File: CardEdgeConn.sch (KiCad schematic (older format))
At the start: 1 part

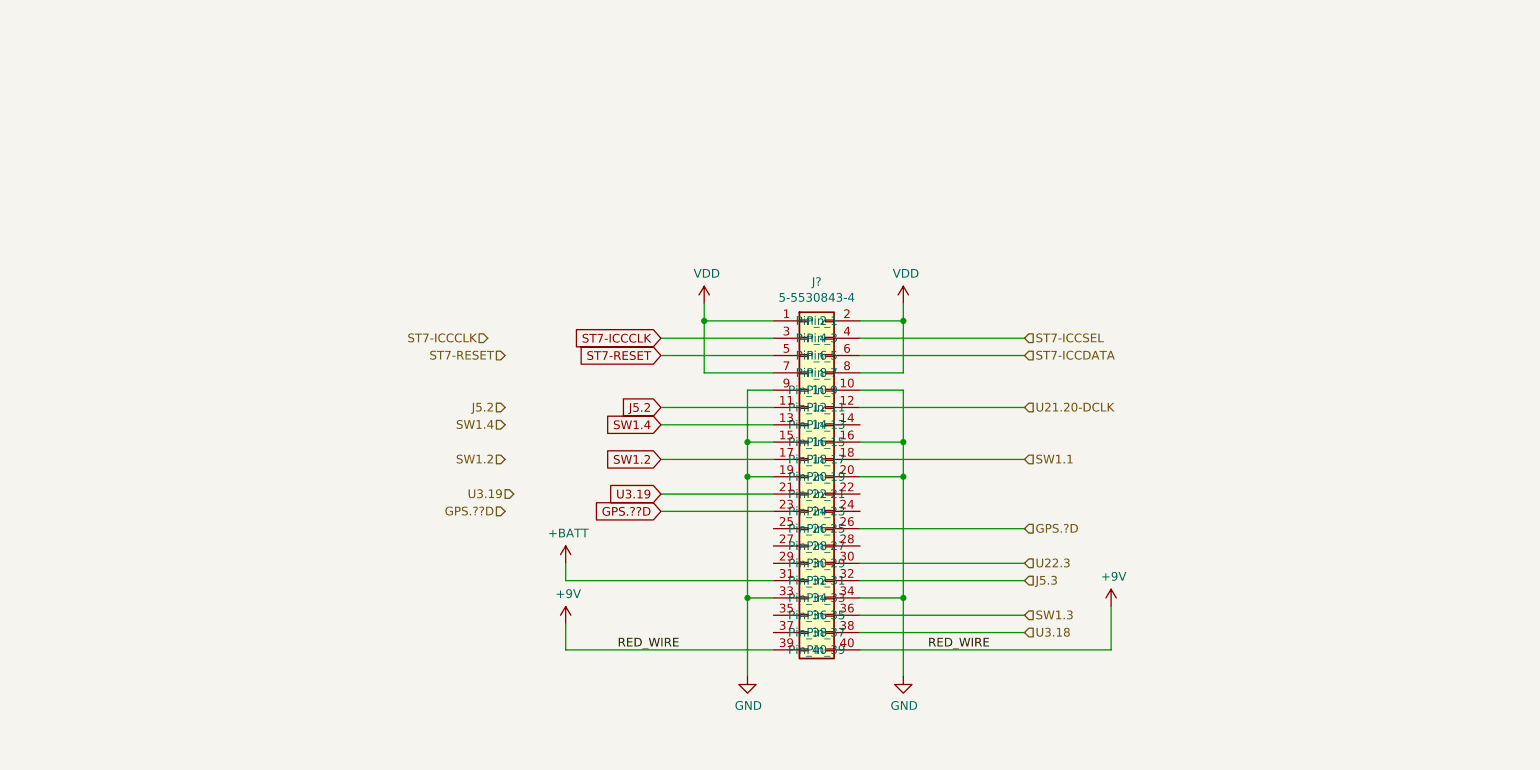
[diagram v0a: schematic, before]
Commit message: Added DC-DC converter
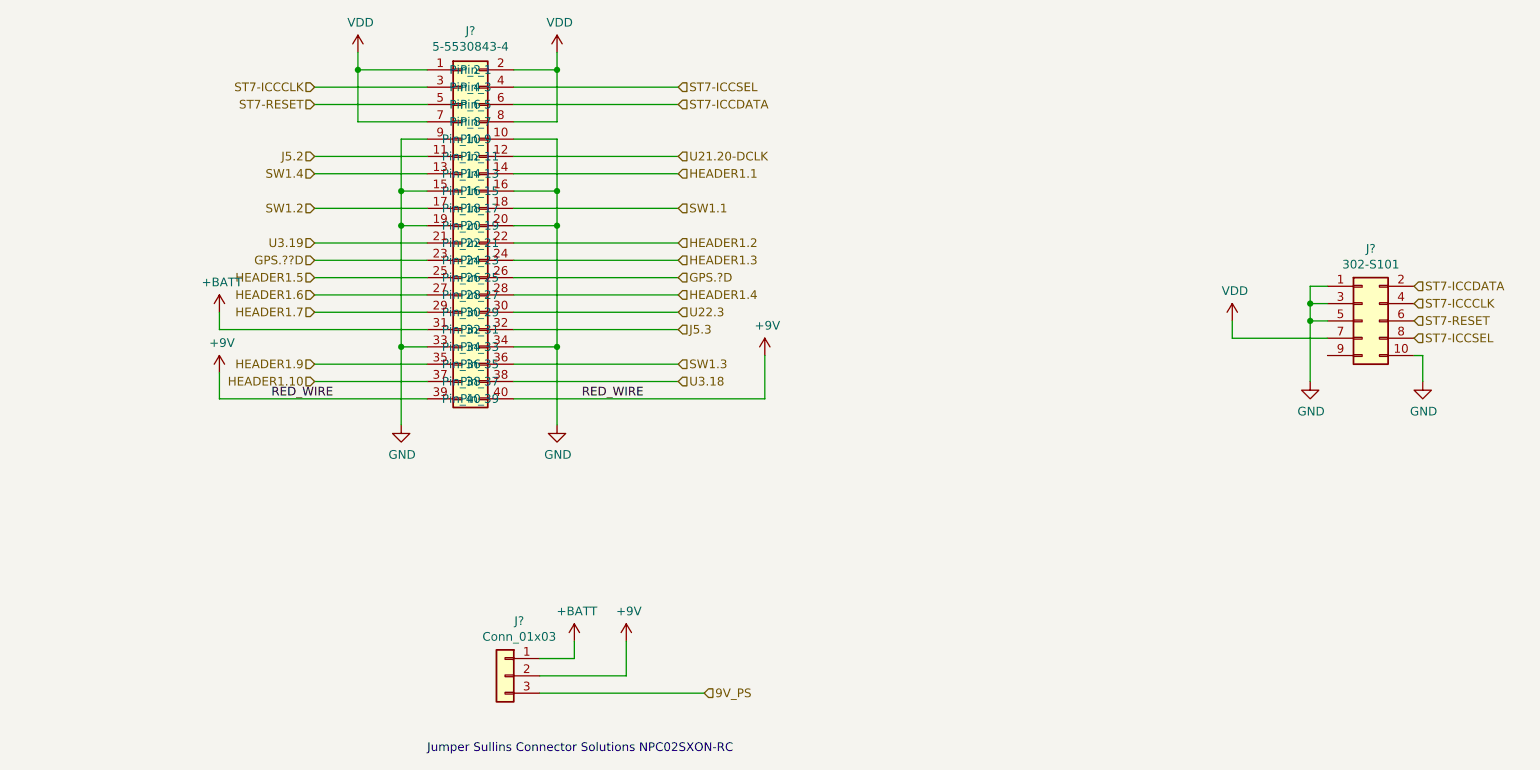
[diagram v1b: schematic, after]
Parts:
- added J?: 302-S101, digikey-footprints:PinHeader_2x5_P2.54mm_Drill1.2mm, symbol Connector_Generic:Conn_02x05_Odd_Even
- added J?: Conn_01x03, symbol Connector_Generic:Conn_01x03
- J?: MPN (none) -> 5-5530843-4; Manufacturer (none) -> TE Connectivity AMP Connectors
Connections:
- net +9V: now also J?.2 (Pin_2)
- net +BATT: now also J?.1 (Pin_1)
- net GND: now also J?.1 (Pin_1), J?.10 (Pin_10), J?.3 (Pin_3), J?.5 (Pin_5)
- net ST7-ICCCLK: now also J?.4 (Pin_4)
- net ST7-ICCDATA: now also J?.2 (Pin_2)
- net ST7-ICCSEL: now also J?.8 (Pin_8)
- net ST7-RESET: now also J?.6 (Pin_6)
- net VDD: now also J?.7 (Pin_7)
- net HEADER1.1: now reaches J?.14 (Pin_14)
- net HEADER1.2: now reaches J?.22 (Pin_22)
- net HEADER1.3: now reaches J?.24 (Pin_24)
- net HEADER1.5: now reaches J?.25 (Pin_25)
- net HEADER1.6: now reaches J?.27 (Pin_27)
- net HEADER1.4: now reaches J?.28 (Pin_28)
- net HEADER1.7: now reaches J?.29 (Pin_29)
- net HEADER1.9: now reaches J?.35 (Pin_35)
- net HEADER1.10: now reaches J?.37 (Pin_37)
- new net 9V_PS: J?.3 (Pin_3)
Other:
- note added: "Jumper Sullins Connector Solutions NPC02SXON-RC"
- moved on the sheet: J?

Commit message: Added libraries used in the project. Top level connections.
Added libraries used in this project to the project folder.

Made additonal top level connections on the top level schematic.
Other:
- note added: "Jumper Sullins Connector Solutions NPC02SXON-RC\nJumper 1-2 to power from LMS6 Battery\nJumper 2-3 to power from exteral power"
- note removed: "Jumper Sullins Connector Solutions NPC02SXON-RC"
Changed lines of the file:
@@
 	4500 4800 3550 4800
 Text Notes 2900 5150 0    50   ~ 0
-Jumper Sullins Connector Solutions NPC02SXON-RC
+Jumper Sullins Connector Solutions NPC02SXON-RC\nJumper 1-2 to power from LMS6 Battery\nJumper 2-3 to power from exteral power
 $EndSCHEMATC

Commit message: Updated EdgeCardConn.sch with GPS UART
Confiremed the GPS UART pins from discord chat.
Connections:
- net GPS.??D renamed GPS.TXD
- net GPS.?D renamed GPS.RXD
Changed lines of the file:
@@
 	2250 2300 2900 2300
 Wire Wire Line
-	1700 2700 2900 2700
-Wire Wire Line
-	1700 2600 1700 2700
+	1500 2600 1500 2700
 $Comp
 L power:+BATT #PWR?
 U 1 1 5F7D097E
-P 1700 2600
+P 1500 2600
 AR Path="/5F7D097E" Ref="#PWR?"  Part="1"
 AR Path="/5F7BE189/5F7D097E" Ref="#PWR?"  Part="1"
 AR Path="/5F7C6408/5F7D097E" Ref="#PWR0103"  Part="1"
-F 0 "#PWR0103" H 1700 2450 50  0001 C CNN
-F 1 "+BATT" H 1715 2773 50  0000 C CNN
-F 2 "" H 1700 2600 50  0001 C CNN
-F 3 "" H 1700 2600 50  0001 C CNN
-	1    1700 2600
+F 0 "#PWR0103" H 1500 2450 50  0001 C CNN
+F 1 "+BATT" H 1515 2773 50  0000 C CNN
+F 2 "" H 1500 2600 50  0001 C CNN
+F 3 "" H 1500 2600 50  0001 C CNN
+	1    1500 2600
 	1    0    0    -1
 $EndComp
@@
 SW1.1
 Text HLabel 4350 2400 2    50   Input ~ 0
-GPS.?D
+GPS.RXD
 Text HLabel 4350 2600 2    50   Input ~ 0
 U22.3
@@
 U3.18
 Text HLabel 2250 2300 0    50   Input ~ 0
-GPS.??D
+GPS.TXD
 Text HLabel 2250 2200 0    50   Input ~ 0
 U3.19
@@
 Text Notes 2900 5150 0    50   ~ 0
 Jumper Sullins Connector Solutions NPC02SXON-RC\nJumper 1-2 to power from LMS6 Battery\nJumper 2-3 to power from exteral power
+Wire Wire Line
+	1500 2700 2900 2700
 $EndSCHEMATC

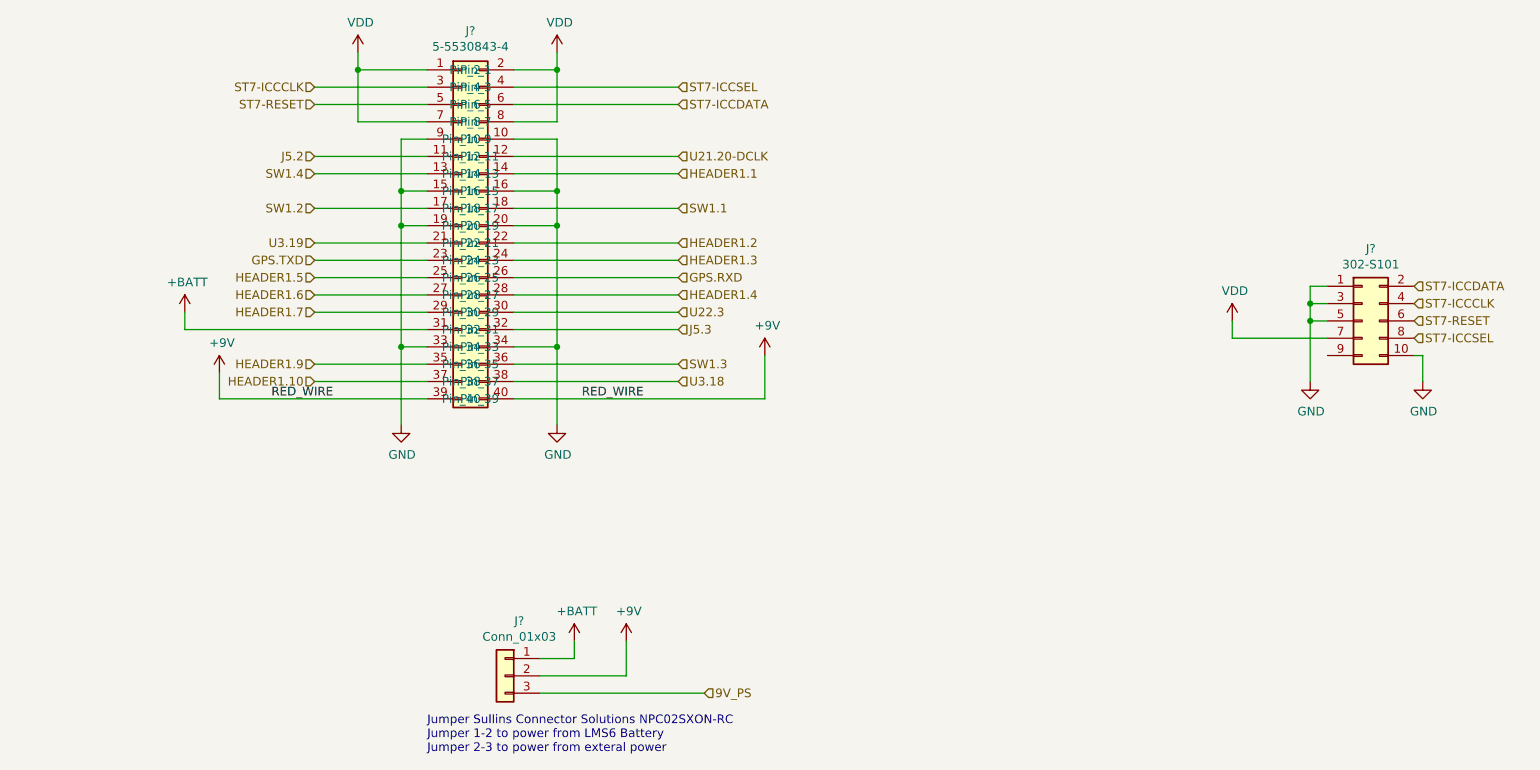
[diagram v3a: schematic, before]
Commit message: Annotated schematics and added UART Jumpers
Annotated schematics.

Added jumpers to GPS UART because I'm still not 100% sure on the connections and I don't want to have to respin a board because I was wrong.
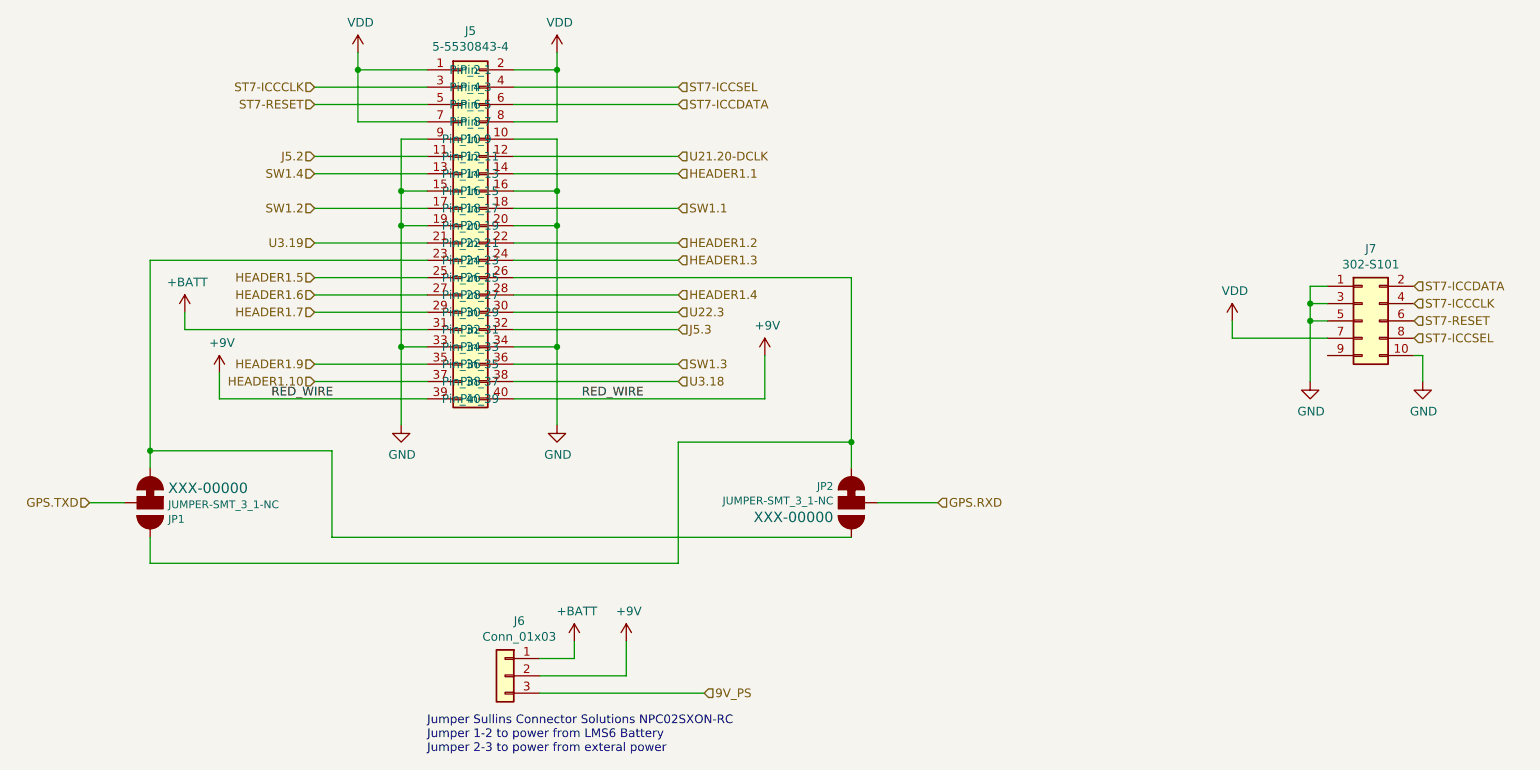
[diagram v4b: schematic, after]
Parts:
- added JP1, JP2: JUMPER-SMT_3_1-NC, SMT-JUMPER_3_1-NC, symbol SparkFun-Jumpers:JUMPER-SMT_3_1-NC
- gave numbers to parts that had none: 3
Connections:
- net GPS.RXD: now also JP2.2; no longer J5.26 (Pin_26)
- net GPS.TXD: now also JP1.2; no longer J5.23 (Pin_23)
- new net: J5.23 (Pin_23), JP1.3, JP2.1
- new net: J5.26 (Pin_26), JP1.1, JP2.3
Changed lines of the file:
@@
 $Descr A4 11693 8268
 encoding utf-8
-Sheet 2 4
+Sheet 4 4
 Title ""
 Date ""
@@
 	3400 2000 4350 2000
 Wire Wire Line
-	3400 2400 4350 2400
-Wire Wire Line
 	3400 2700 4350 2700
 Wire Wire Line
@@
 	2250 2200 2900 2200
 Wire Wire Line
-	2250 2300 2900 2300
-Wire Wire Line
 	1500 2600 1500 2700
 $Comp
@@
 AR Path="/5F7D09C4" Ref="J?"  Part="1"
 AR Path="/5F7BE189/5F7D09C4" Ref="J?"  Part="1"
-AR Path="/5F7C6408/5F7D09C4" Ref="J?"  Part="1"
-F 0 "J?" H 3150 5425 50  0000 C CNN
+AR Path="/5F7C6408/5F7D09C4" Ref="J5"  Part="1"
+F 0 "J5" H 3150 5425 50  0000 C CNN
 F 1 "5-5530843-4" H 3150 5334 50  0000 C CNN
 F 2 "" H 3150 3200 50  0001 C CNN
@@
 Text HLabel 4350 2000 2    50   Input ~ 0
 SW1.1
-Text HLabel 4350 2400 2    50   Input ~ 0
+Text HLabel 5850 3700 2    50   Input ~ 0
 GPS.RXD
 Text HLabel 4350 2600 2    50   Input ~ 0
@@
 Text HLabel 4350 3000 2    50   Input ~ 0
 U3.18
-Text HLabel 2250 2300 0    50   Input ~ 0
+Text HLabel 950  3700 0    50   Input ~ 0
 GPS.TXD
 Text HLabel 2250 2200 0    50   Input ~ 0
@@
 ST7-ICCCLK
 $Comp
-L Connector_Generic:Conn_02x05_Odd_Even J?
+L Connector_Generic:Conn_02x05_Odd_Even J7
 U 1 1 5F836EA0
 P 8300 2650
-F 0 "J?" H 8350 3067 50  0000 C CNN
+F 0 "J7" H 8350 3067 50  0000 C CNN
 F 1 "302-S101" H 8350 2976 50  0000 C CNN
 F 2 "digikey-footprints:PinHeader_2x5_P2.54mm_Drill1.2mm" H 8300 2650 50  0001 C CNN
@@
 AR Path="/5F83EE0B" Ref="#PWR?"  Part="1"
 AR Path="/5F7BE189/5F83EE0B" Ref="#PWR?"  Part="1"
-AR Path="/5F7C6408/5F83EE0B" Ref="#PWR?"  Part="1"
-F 0 "#PWR?" H 7550 2500 50  0001 C CNN
+AR Path="/5F7C6408/5F83EE0B" Ref="#PWR015"  Part="1"
+F 0 "#PWR015" H 7550 2500 50  0001 C CNN
 F 1 "VDD" H 7565 2823 50  0000 C CNN
 F 2 "" H 7550 2650 50  0001 C CNN
@@
 AR Path="/5F840CF8" Ref="#PWR?"  Part="1"
 AR Path="/5F7BE189/5F840CF8" Ref="#PWR?"  Part="1"
-AR Path="/5F7C6408/5F840CF8" Ref="#PWR?"  Part="1"
-F 0 "#PWR?" H 8000 2750 50  0001 C CNN
+AR Path="/5F7C6408/5F840CF8" Ref="#PWR016"  Part="1"
+F 0 "#PWR016" H 8000 2750 50  0001 C CNN
 F 1 "GND" H 8005 2827 50  0000 C CNN
 F 2 "" H 8000 3000 50  0001 C CNN
@@
 AR Path="/5F845227" Ref="#PWR?"  Part="1"
 AR Path="/5F7BE189/5F845227" Ref="#PWR?"  Part="1"
-AR Path="/5F7C6408/5F845227" Ref="#PWR?"  Part="1"
-F 0 "#PWR?" H 8650 2750 50  0001 C CNN
+AR Path="/5F7C6408/5F845227" Ref="#PWR017"  Part="1"
+F 0 "#PWR017" H 8650 2750 50  0001 C CNN
 F 1 "GND" H 8655 2827 50  0000 C CNN
 F 2 "" H 8650 3000 50  0001 C CNN
@@
 AR Path="/5F8BD332" Ref="#PWR?"  Part="1"
 AR Path="/5F7BE189/5F8BD332" Ref="#PWR?"  Part="1"
-AR Path="/5F7C6408/5F8BD332" Ref="#PWR?"  Part="1"
-F 0 "#PWR?" H 4050 4350 50  0001 C CNN
+AR Path="/5F7C6408/5F8BD332" Ref="#PWR014"  Part="1"
+F 0 "#PWR014" H 4050 4350 50  0001 C CNN
 F 1 "+9V" H 4065 4673 50  0000 C CNN
 F 2 "" H 4050 4500 50  0001 C CNN
@@
 AR Path="/5F8C0163" Ref="#PWR?"  Part="1"
 AR Path="/5F7BE189/5F8C0163" Ref="#PWR?"  Part="1"
-AR Path="/5F7C6408/5F8C0163" Ref="#PWR?"  Part="1"
-F 0 "#PWR?" H 3750 4350 50  0001 C CNN
+AR Path="/5F7C6408/5F8C0163" Ref="#PWR013"  Part="1"
+F 0 "#PWR013" H 3750 4350 50  0001 C CNN
 F 1 "+BATT" H 3765 4673 50  0000 C CNN
 F 2 "" H 3750 4500 50  0001 C CNN
@@
 	3750 4600 3550 4600
 $Comp
-L Connector_Generic:Conn_01x03 J?
+L Connector_Generic:Conn_01x03 J6
 U 1 1 5F8CD356
 P 3350 4700
-F 0 "J?" H 3268 5017 50  0000 C CNN
+F 0 "J6" H 3268 5017 50  0000 C CNN
 F 1 "Conn_01x03" H 3268 4926 50  0000 C CNN
 F 2 "" H 3350 4700 50  0001 C CNN
@@
 Wire Wire Line
 	1500 2700 2900 2700
+$Comp
+L SparkFun-Jumpers:JUMPER-SMT_3_1-NC JP1
+U 1 1 5F8B7A4C
+P 1300 3700
+F 0 "JP1" H 1404 3795 45  0000 L CNN
+F 1 "JUMPER-SMT_3_1-NC" H 1404 3711 45  0000 L CNN
+F 2 "SMT-JUMPER_3_1-NC" H 1300 3950 20  0001 C CNN
+F 3 "" V 1300 3645 60  0001 C CNN
+F 4 "XXX-00000" H 1404 3616 60  0000 L CNN "PROD_ID"
+	1    1300 3700
+	1    0    0    1
+$EndComp
+$Comp
+L SparkFun-Jumpers:JUMPER-SMT_3_1-NC JP2
+U 1 1 5F8B9EA1
+P 5350 3700
+F 0 "JP2" H 5454 3605 45  0000 L CNN
+F 1 "JUMPER-SMT_3_1-NC" H 5454 3689 45  0000 L CNN
+F 2 "SMT-JUMPER_3_1-NC" H 5350 3950 20  0001 C CNN
+F 3 "" V 5350 3645 60  0001 C CNN
+F 4 "XXX-00000" H 5454 3784 60  0000 L CNN "PROD_ID"
+	1    5350 3700
+	-1   0    0    1
+$EndComp
+Wire Wire Line
+	950  3700 1150 3700
+Wire Wire Line
+	1300 3500 1300 3400
+Wire Wire Line
+	1300 2300 2900 2300
+Wire Wire Line
+	5500 3700 5850 3700
+Wire Wire Line
+	5350 3500 5350 3350
+Wire Wire Line
+	5350 2400 3400 2400
+Wire Wire Line
+	5350 3900 2350 3900
+Wire Wire Line
+	2350 3900 2350 3400
+Wire Wire Line
+	2350 3400 1300 3400
+Connection ~ 1300 3400
+Wire Wire Line
+	1300 3400 1300 2300
+Wire Wire Line
+	1300 3900 1300 4050
+Wire Wire Line
+	1300 4050 4350 4050
+Wire Wire Line
+	4350 4050 4350 3350
+Wire Wire Line
+	4350 3350 5350 3350
+Connection ~ 5350 3350
+Wire Wire Line
+	5350 3350 5350 2400
 $EndSCHEMATC
